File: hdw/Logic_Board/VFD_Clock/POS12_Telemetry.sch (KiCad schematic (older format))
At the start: 9 parts

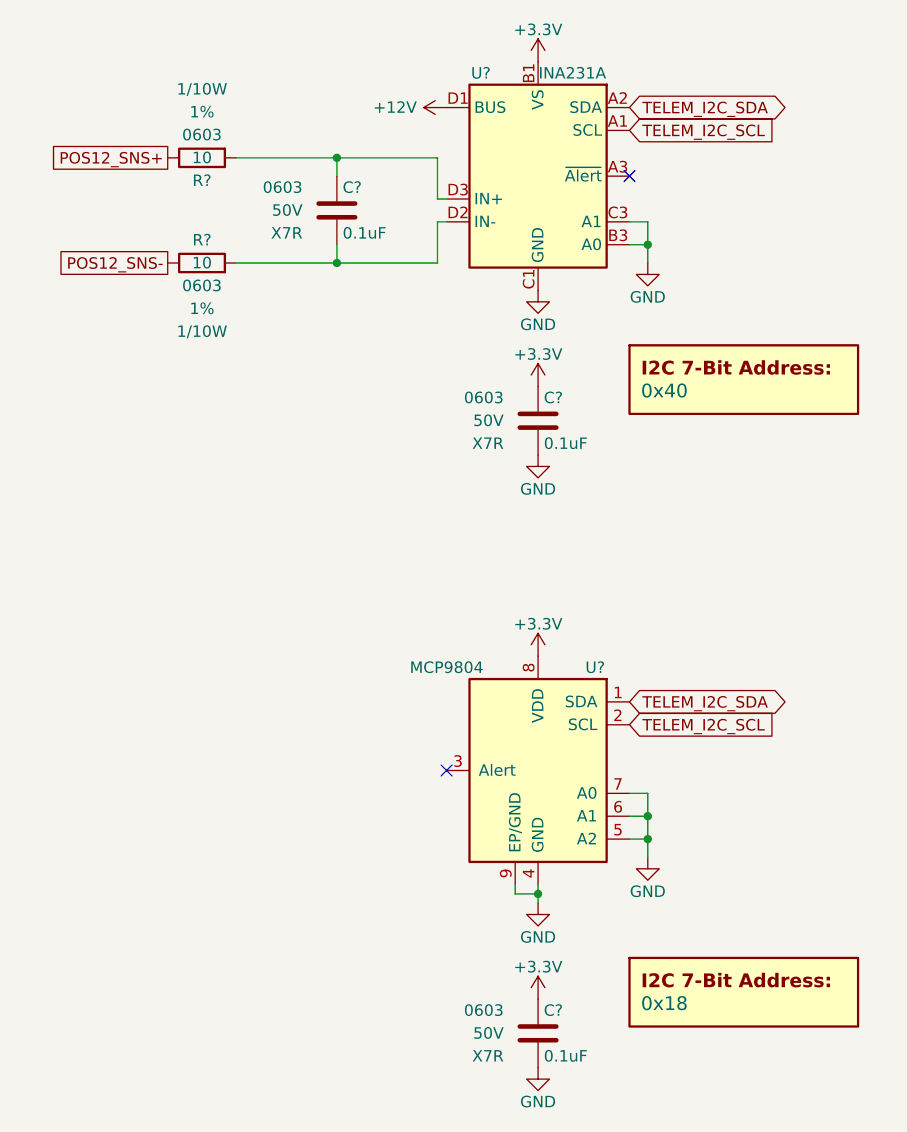
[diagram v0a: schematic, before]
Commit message: Lots of schematic additions
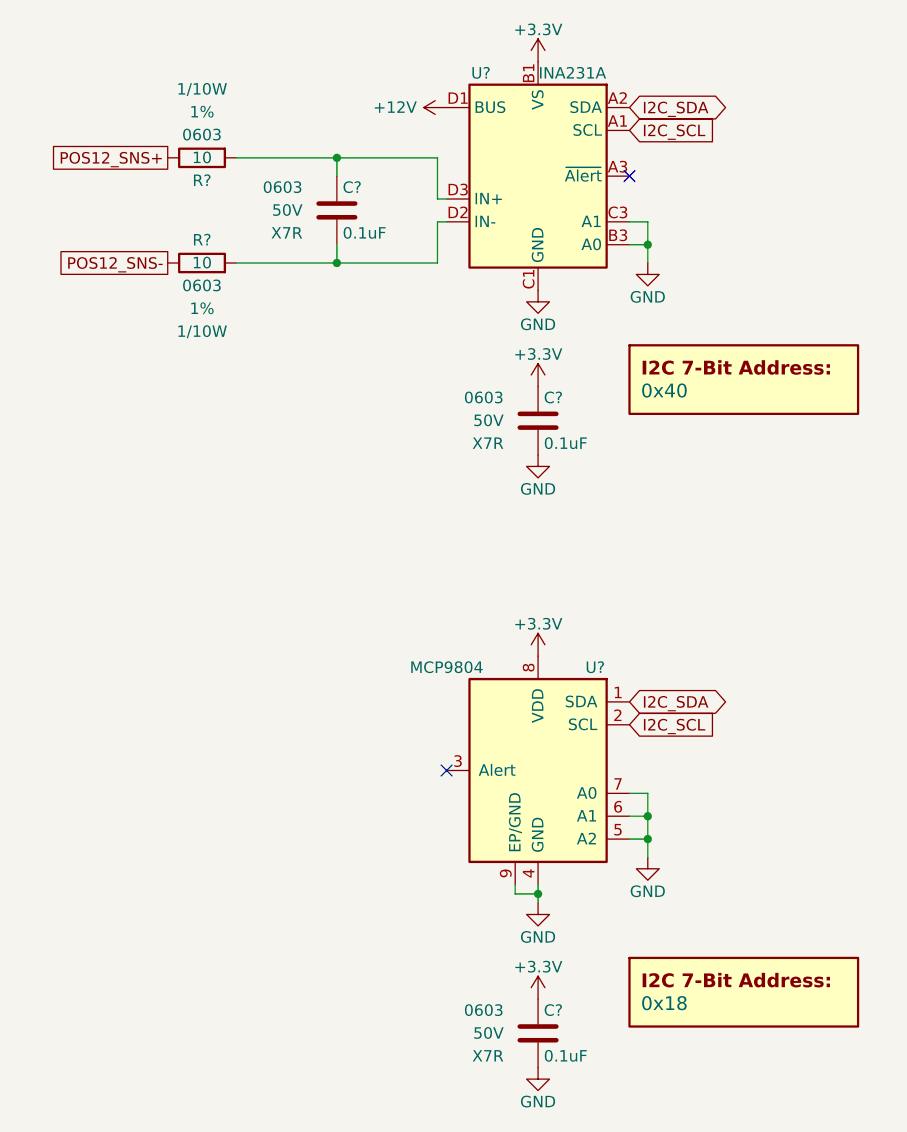
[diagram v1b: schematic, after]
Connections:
- net TELEM_I2C_SCL renamed I2C_SCL
- net TELEM_I2C_SDA renamed I2C_SDA
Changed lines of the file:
@@
 $Descr A 11000 8500
 encoding utf-8
-Sheet 26 26
+Sheet 17 28
 Title ""
 Date ""
@@
 $EndComp
 Text GLabel 5510 1740 2    50   Input ~ 0
-TELEM_I2C_SCL
+I2C_SCL
 $Comp
 L Custom_Library:C_Custom C?
@@
 $EndComp
 Text GLabel 5510 1640 2    50   BiDi ~ 0
-TELEM_I2C_SDA
+I2C_SDA
 NoConn ~ 5510 1940
 $Comp
@@
 $EndComp
 Text GLabel 5510 4340 2    50   Input ~ 0
-TELEM_I2C_SCL
+I2C_SCL
 Text GLabel 5510 4240 2    50   BiDi ~ 0
-TELEM_I2C_SDA
+I2C_SDA
 NoConn ~ 4710 4540
 $Comp

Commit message: Added backup RTC, IO connector, other stuff
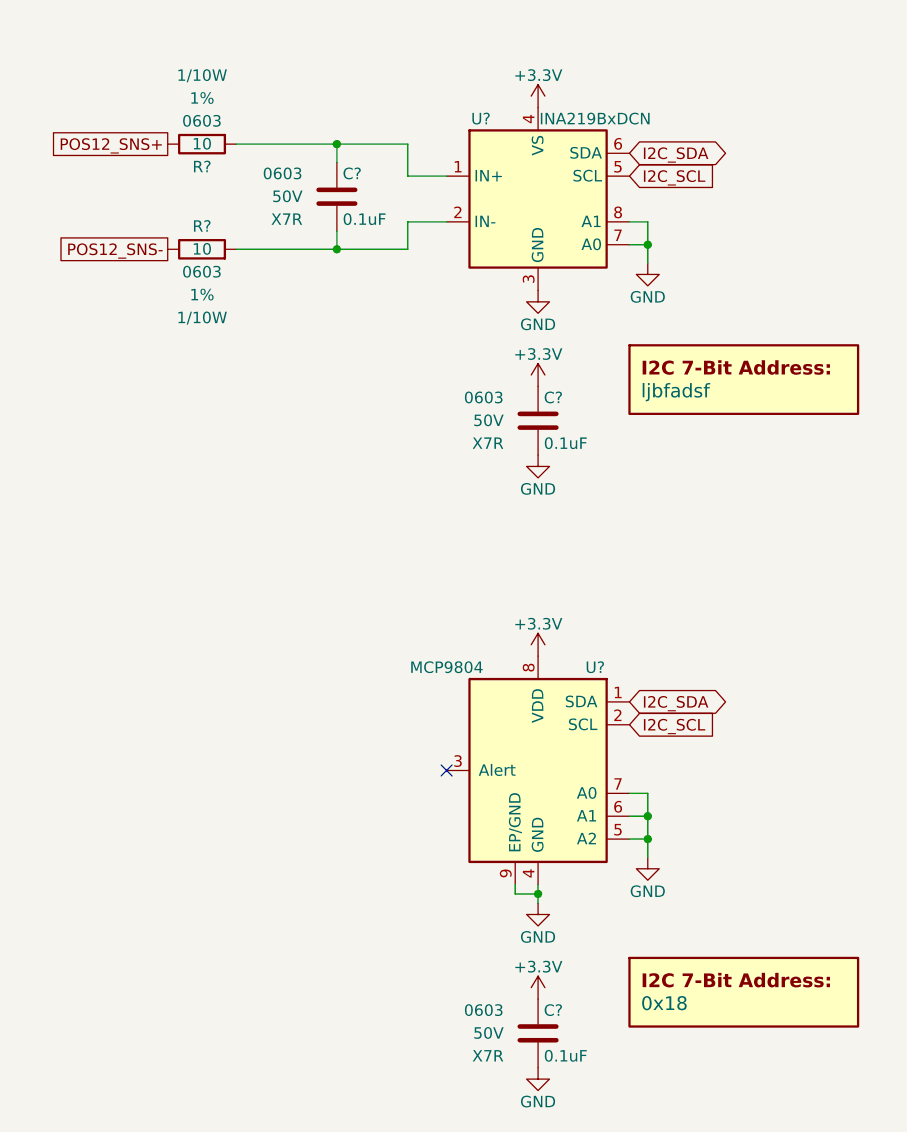
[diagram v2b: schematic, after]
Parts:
- removed U?: INA231A, Custom Footprints Library:Texas_DSBGA-12_1.65x1.39mm_Layout3x4_P0.4mm, symbol Custom_Library:INA231A
- added U?: INA219BxDCN, Package_TO_SOT_SMD:SOT-23-8, symbol Analog_ADC:INA219BxDCN
- DOC?: value 0x40 -> ljbfadsf
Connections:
- net +3V3: now also U?.4 (VS)
- net GND: now also U?.3 (GND), U?.7 (A0), U?.8 (A1)
- net I2C_SCL: now also U?.5 (SCL)
- net I2C_SDA: now also U?.6 (SDA)
- net at C?.2, R?.1: now also U?.2 (IN-)
- net at C?.1, R?.1: now also U?.1 (IN+)
- no-connect marks 2 -> 1
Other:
- moved on the sheet: C?, R?
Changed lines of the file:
@@
 $Descr A 11000 8500
 encoding utf-8
-Sheet 17 28
+Sheet 17 29
 Title ""
 Date ""
@@
 Comment4 ""
 $EndDescr
-$Comp
-L Custom_Library:INA231A U?
-U 1 1 5E073058
-P 5110 1940
-AR Path="/5E0652BA/5E073058" Ref="U?"  Part="1"
-AR Path="/5E0A0E29/5E073058" Ref="U?"  Part="1"
-AR Path="/5E052856/5E073058" Ref="U?"  Part="1"
-F 0 "U?" H 4860 2390 50  0000 C CNN
-F 1 "INA231A" H 5260 2390 50  0000 C CNN
-F 2 "Custom Footprints Library:Texas_DSBGA-12_1.65x1.39mm_Layout3x4_P0.4mm" H 5910 1490 50  0001 C CNN
-F 3 "http://www.ti.com/lit/ds/symlink/ina231.pdf" H 5460 1840 50  0001 C CNN
-F 4 "296-41263-1-ND" H 5110 1940 50  0001 C CNN "Digi-Key PN"
-	1    5110 1940
-	1    0    0    -1
-$EndComp
-Text GLabel 3490 1860 0    50   UnSpc ~ 0
+Text GLabel 3490 1800 0    50   UnSpc ~ 0
 POS12_SNS+
-Text GLabel 3490 2320 0    50   UnSpc ~ 0
+Text GLabel 3490 2260 0    50   UnSpc ~ 0
 POS12_SNS-
 $Comp
@@
 L power:+3.3V #PWR?
 U 1 1 5E0AD665
-P 5110 1440
+P 5110 1640
 AR Path="/5E0652BA/5E0AD665" Ref="#PWR?"  Part="1"
 AR Path="/5E0A0E29/5E0AD665" Ref="#PWR?"  Part="1"
 AR Path="/5E052856/5E0AD665" Ref="#PWR?"  Part="1"
-F 0 "#PWR?" H 5110 1290 50  0001 C CNN
-F 1 "+3.3V" H 5110 1580 50  0000 C CNN
-F 2 "" H 5110 1440 50  0001 C CNN
-F 3 "" H 5110 1440 50  0001 C CNN
-	1    5110 1440
-	1    0    0    -1
-$EndComp
-$Comp
-L power:+12V #PWR?
-U 1 1 5E0AD80E
-P 4710 1640
-AR Path="/5E0652BA/5E0AD80E" Ref="#PWR?"  Part="1"
-AR Path="/5E0A0E29/5E0AD80E" Ref="#PWR?"  Part="1"
-AR Path="/5E052856/5E0AD80E" Ref="#PWR?"  Part="1"
-F 0 "#PWR?" H 4710 1490 50  0001 C CNN
-F 1 "+12V" V 4710 1770 50  0000 L CNN
-F 2 "" H 4710 1640 50  0001 C CNN
-F 3 "" H 4710 1640 50  0001 C CNN
-	1    4710 1640
-	0    -1   -1   0
-$EndComp
-Text GLabel 5510 1740 2    50   Input ~ 0
+F 0 "#PWR?" H 5110 1490 50  0001 C CNN
+F 1 "+3.3V" H 5110 1780 50  0000 C CNN
+F 2 "" H 5110 1640 50  0001 C CNN
+F 3 "" H 5110 1640 50  0001 C CNN
+	1    5110 1640
+	1    0    0    -1
+$EndComp
+Text GLabel 5510 1940 2    50   Input ~ 0
 I2C_SCL
 $Comp
@@
 	1    0    0    -1
 $EndComp
-Text GLabel 5510 1640 2    50   BiDi ~ 0
+Text GLabel 5510 1840 2    50   BiDi ~ 0
 I2C_SDA
-NoConn ~ 5510 1940
 $Comp
 L Custom_Library:I2C_Address DOC?
@@
 AR Path="/5E052856/5E0B8BC8" Ref="DOC?"  Part="1"
 F 0 "DOC?" H 6010 3130 60  0001 C CNN
-F 1 "0x40" H 5560 2880 60  0000 L CNN
+F 1 "ljbfadsf" H 5560 2880 60  0000 L CNN
 F 2 "" H 6010 3230 60  0001 C CNN
 F 3 "" H 6010 3230 60  0001 C CNN
@@
 	5590 4840 5590 4740
 Wire Wire Line
-	4230 2320 4230 2240
-Wire Wire Line
-	4230 1940 4230 1860
-Wire Wire Line
-	4230 2320 4670 2320
-Wire Wire Line
-	4670 2320 4670 2140
-Wire Wire Line
-	4670 2140 4710 2140
-Connection ~ 4230 2320
-Wire Wire Line
-	4230 1860 4670 1860
-Wire Wire Line
-	4670 1860 4670 2040
-Wire Wire Line
-	4670 2040 4710 2040
+	4230 2260 4230 2180
+Wire Wire Line
+	4230 1880 4230 1800
 $Comp
 L Custom_Library:C_Custom C?
 U 1 1 5E07E0FD
-P 4230 2090
+P 4230 2030
 AR Path="/5B3E071A/5E07E0FD" Ref="C?"  Part="1"
 AR Path="/5E0652BA/5E07E0FD" Ref="C?"  Part="1"
 AR Path="/5E0A0E29/5E07E0FD" Ref="C?"  Part="1"
 AR Path="/5E052856/5E07E0FD" Ref="C?"  Part="1"
-F 0 "C?" H 4255 2190 50  0000 L CNN
-F 1 "0.1uF" H 4255 1990 50  0000 L CNN
-F 2 "Capacitors_SMD:C_0603" H 4268 1940 50  0001 C CNN
-F 3 "" H 4255 2190 50  0001 C CNN
-F 4 "0603" H 4080 2190 50  0000 R CNN "display_footprint"
-F 5 "50V" H 4080 2090 50  0000 R CNN "Voltage"
-F 6 "X7R" H 4080 1990 50  0000 R CNN "Dielectric"
-F 7 "399-6856-1-ND" H 320 -4790 50  0001 C CNN "Digi-Key PN"
-	1    4230 2090
+F 0 "C?" H 4255 2130 50  0000 L CNN
+F 1 "0.1uF" H 4255 1930 50  0000 L CNN
+F 2 "Capacitors_SMD:C_0603" H 4268 1880 50  0001 C CNN
+F 3 "" H 4255 2130 50  0001 C CNN
+F 4 "0603" H 4080 2130 50  0000 R CNN "display_footprint"
+F 5 "50V" H 4080 2030 50  0000 R CNN "Voltage"
+F 6 "X7R" H 4080 1930 50  0000 R CNN "Dielectric"
+F 7 "399-6856-1-ND" H 320 -4850 50  0001 C CNN "Digi-Key PN"
+	1    4230 2030
 	1    0    0    -1
 $EndComp
@@
 L Custom_Library:R_Custom R?
 U 1 1 5E082EBB
-P 3640 2320
+P 3640 2260
 AR Path="/5CB6F1ED/5E082EBB" Ref="R?"  Part="1"
 AR Path="/5E0652BA/5E082EBB" Ref="R?"  Part="1"
 AR Path="/5E0A0E29/5E082EBB" Ref="R?"  Part="1"
 AR Path="/5E052856/5E082EBB" Ref="R?"  Part="1"
-F 0 "R?" V 3540 2320 50  0000 C CNN
-F 1 "10" V 3640 2320 50  0000 C CNN
-F 2 "Resistors_SMD:R_0603" H 3640 2320 50  0001 C CNN
-F 3 "" H 3640 2320 50  0001 C CNN
-F 4 "YAG3351CT-ND" H 3940 2720 60  0001 C CNN "Digi-Key PN"
-F 5 "0603" V 3740 2320 50  0000 C CNN "display_footprint"
-F 6 "1%" V 3840 2320 50  0000 C CNN "Tolerance"
-F 7 "1/10W" V 3940 2320 50  0000 C CNN "Wattage"
-	1    3640 2320
+F 0 "R?" V 3540 2260 50  0000 C CNN
+F 1 "10" V 3640 2260 50  0000 C CNN
+F 2 "Resistors_SMD:R_0603" H 3640 2260 50  0001 C CNN
+F 3 "" H 3640 2260 50  0001 C CNN
+F 4 "YAG3351CT-ND" H 3940 2660 60  0001 C CNN "Digi-Key PN"
+F 5 "0603" V 3740 2260 50  0000 C CNN "display_footprint"
+F 6 "1%" V 3840 2260 50  0000 C CNN "Tolerance"
+F 7 "1/10W" V 3940 2260 50  0000 C CNN "Wattage"
+	1    3640 2260
 	0    1    1    0
 $EndComp
 Wire Wire Line
-	3790 2320 4230 2320
+	3790 2260 4230 2260
 $Comp
 L Custom_Library:R_Custom R?
 U 1 1 5E083C4C
-P 3640 1860
+P 3640 1800
 AR Path="/5CB6F1ED/5E083C4C" Ref="R?"  Part="1"
 AR Path="/5E0652BA/5E083C4C" Ref="R?"  Part="1"
 AR Path="/5E0A0E29/5E083C4C" Ref="R?"  Part="1"
 AR Path="/5E052856/5E083C4C" Ref="R?"  Part="1"
-F 0 "R?" V 3540 1860 50  0000 C CNN
-F 1 "10" V 3640 1860 50  0000 C CNN
-F 2 "Resistors_SMD:R_0603" H 3640 1860 50  0001 C CNN
-F 3 "" H 3640 1860 50  0001 C CNN
-F 4 "YAG3351CT-ND" H 3940 2260 60  0001 C CNN "Digi-Key PN"
-F 5 "0603" V 3740 1860 50  0000 C CNN "display_footprint"
-F 6 "1%" V 3840 1860 50  0000 C CNN "Tolerance"
-F 7 "1/10W" V 3940 1860 50  0000 C CNN "Wattage"
-	1    3640 1860
+F 0 "R?" V 3540 1800 50  0000 C CNN
+F 1 "10" V 3640 1800 50  0000 C CNN
+F 2 "Resistors_SMD:R_0603" H 3640 1800 50  0001 C CNN
+F 3 "" H 3640 1800 50  0001 C CNN
+F 4 "YAG3351CT-ND" H 3940 2200 60  0001 C CNN "Digi-Key PN"
+F 5 "0603" V 3740 1800 50  0000 C CNN "display_footprint"
+F 6 "1%" V 3840 1800 50  0000 C CNN "Tolerance"
+F 7 "1/10W" V 3940 1800 50  0000 C CNN "Wattage"
+	1    3640 1800
 	0    1    -1   0
 $EndComp
 Wire Wire Line
-	3790 1860 4230 1860
-Connection ~ 4230 1860
+	3790 1800 4230 1800
+$Comp
+L Analog_ADC:INA219BxDCN U?
+U 1 1 5E1AAC3C
+P 5110 2040
+F 0 "U?" H 4860 2390 50  0000 C CNN
+F 1 "INA219BxDCN" H 5360 2390 50  0000 C CNN
+F 2 "Package_TO_SOT_SMD:SOT-23-8" H 5760 1690 50  0001 C CNN
+F 3 "http://www.ti.com/lit/ds/symlink/ina219.pdf" H 5460 1940 50  0001 C CNN
+F 4 "296-46420-1-ND" H 5110 2040 50  0001 C CNN "Digi-Key PN"
+	1    5110 2040
+	1    0    0    -1
+$EndComp
+Wire Wire Line
+	4710 1940 4540 1940
+Wire Wire Line
+	4540 1940 4540 1800
+Wire Wire Line
+	4540 1800 4230 1800
+Connection ~ 4230 1800
+Wire Wire Line
+	4710 2140 4540 2140
+Wire Wire Line
+	4540 2140 4540 2260
+Wire Wire Line
+	4540 2260 4230 2260
+Connection ~ 4230 2260
 $EndSCHEMATC

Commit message: Changed to configurable discrete gates, added VBAT stuff
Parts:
- removed C?: 0.1uF, Capacitors_SMD:C_0603, symbol Custom_Library:C_Custom
- removed DOC?: 0x18, symbol Custom_Library:I2C_Address
- removed U?: MCP9804, Package_DFN_QFN:DFN-8-1EP_3x2mm_P0.5mm_EP1.3x1.5mm, symbol Sensor_Temperature:MCP9804_DFN
- added C?: 0.1uF, Capacitors_SMD:C_0603, symbol Custom_Library:C_Custom
- added DOC?: 0x18, symbol Custom_Library:I2C_Address
- added U?: MCP9804, Package_DFN_QFN:DFN-8-1EP_3x2mm_P0.5mm_EP1.3x1.5mm, symbol Sensor_Temperature:MCP9804_DFN
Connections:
- net +3V3: now also C?.1, U?.8 (VDD)
- net GND: now also C?.2, U?.4 (GND), U?.5 (A2), U?.6 (A1), U?.7 (A0), U?.9 (EP/GND)
- net I2C_SCL: now also U?.2 (SCL)
- net I2C_SDA: now also U?.1 (SDA)
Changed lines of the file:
@@
 $Comp
 L power:GND #PWR?
-U 1 1 5E0BDB8A
+U 1 1 5E2AA995
 P 5110 5120
-AR Path="/5B3E071A/5E0BDB8A" Ref="#PWR?"  Part="1"
-AR Path="/5E0652BA/5E0BDB8A" Ref="#PWR?"  Part="1"
-AR Path="/5E0A0E29/5E0BDB8A" Ref="#PWR?"  Part="1"
-AR Path="/5E052856/5E0BDB8A" Ref="#PWR?"  Part="1"
+AR Path="/5B3E071A/5E2AA995" Ref="#PWR?"  Part="1"
+AR Path="/5E0652BA/5E2AA995" Ref="#PWR?"  Part="1"
+AR Path="/5E0A0E29/5E2AA995" Ref="#PWR?"  Part="1"
+AR Path="/5E052856/5E2AA995" Ref="#PWR?"  Part="1"
 F 0 "#PWR?" H 5110 4870 50  0001 C CNN
 F 1 "GND" H 5110 4970 50  0000 C CNN
@@
 $Comp
 L power:+3.3V #PWR?
-U 1 1 5E0BDB95
+U 1 1 5E2AA99A
 P 5110 4040
-AR Path="/5E0652BA/5E0BDB95" Ref="#PWR?"  Part="1"
-AR Path="/5E0A0E29/5E0BDB95" Ref="#PWR?"  Part="1"
-AR Path="/5E052856/5E0BDB95" Ref="#PWR?"  Part="1"
+AR Path="/5E0652BA/5E2AA99A" Ref="#PWR?"  Part="1"
+AR Path="/5E0A0E29/5E2AA99A" Ref="#PWR?"  Part="1"
+AR Path="/5E052856/5E2AA99A" Ref="#PWR?"  Part="1"
 F 0 "#PWR?" H 5110 3890 50  0001 C CNN
 F 1 "+3.3V" H 5110 4180 50  0000 C CNN
@@
 $Comp
 L Sensor_Temperature:MCP9804_DFN U?
-U 1 1 5E0BDB9D
+U 1 1 5E2AA99D
 P 5110 4540
-AR Path="/5B3E071A/5E0BDB9D" Ref="U?"  Part="1"
-AR Path="/5E0652BA/5E0BDB9D" Ref="U?"  Part="1"
-AR Path="/5E0A0E29/5E0BDB9D" Ref="U?"  Part="1"
-AR Path="/5E052856/5E0BDB9D" Ref="U?"  Part="1"
+AR Path="/5B3E071A/5E2AA99D" Ref="U?"  Part="1"
+AR Path="/5E0652BA/5E2AA99D" Ref="U?"  Part="1"
+AR Path="/5E0A0E29/5E2AA99D" Ref="U?"  Part="1"
+AR Path="/5E052856/5E2AA99D" Ref="U?"  Part="1"
 F 0 "U?" H 4860 4990 50  0000 C CNN
 F 1 "MCP9804" H 5510 4990 50  0000 C CNN
@@
 $Comp
 L Custom_Library:C_Custom C?
-U 1 1 5E0CB7AA
+U 1 1 5E2AA9A1
 P 5110 5690
-AR Path="/5B3E071A/5E0CB7AA" Ref="C?"  Part="1"
-AR Path="/5E0652BA/5E0CB7AA" Ref="C?"  Part="1"
-AR Path="/5E0A0E29/5E0CB7AA" Ref="C?"  Part="1"
-AR Path="/5E052856/5E0CB7AA" Ref="C?"  Part="1"
+AR Path="/5B3E071A/5E2AA9A1" Ref="C?"  Part="1"
+AR Path="/5E0652BA/5E2AA9A1" Ref="C?"  Part="1"
+AR Path="/5E0A0E29/5E2AA9A1" Ref="C?"  Part="1"
+AR Path="/5E052856/5E2AA9A1" Ref="C?"  Part="1"
 F 0 "C?" H 5135 5790 50  0000 L CNN
 F 1 "0.1uF" H 5135 5590 50  0000 L CNN
@@
 $Comp
 L power:+3.3V #PWR?
-U 1 1 5E0CB7B0
+U 1 1 5E2AA9A6
 P 5110 5540
-AR Path="/5E0652BA/5E0CB7B0" Ref="#PWR?"  Part="1"
-AR Path="/5E0A0E29/5E0CB7B0" Ref="#PWR?"  Part="1"
-AR Path="/5E052856/5E0CB7B0" Ref="#PWR?"  Part="1"
+AR Path="/5E0652BA/5E2AA9A6" Ref="#PWR?"  Part="1"
+AR Path="/5E0A0E29/5E2AA9A6" Ref="#PWR?"  Part="1"
+AR Path="/5E052856/5E2AA9A6" Ref="#PWR?"  Part="1"
 F 0 "#PWR?" H 5110 5390 50  0001 C CNN
 F 1 "+3.3V" H 5110 5680 50  0000 C CNN
@@
 $Comp
 L power:GND #PWR?
-U 1 1 5E0CB7B6
+U 1 1 5E2AA9AD
 P 5110 5840
-AR Path="/5E0652BA/5E0CB7B6" Ref="#PWR?"  Part="1"
-AR Path="/5E0A0E29/5E0CB7B6" Ref="#PWR?"  Part="1"
-AR Path="/5E052856/5E0CB7B6" Ref="#PWR?"  Part="1"
+AR Path="/5E0652BA/5E2AA9AD" Ref="#PWR?"  Part="1"
+AR Path="/5E0A0E29/5E2AA9AD" Ref="#PWR?"  Part="1"
+AR Path="/5E052856/5E2AA9AD" Ref="#PWR?"  Part="1"
 F 0 "#PWR?" H 5110 5590 50  0001 C CNN
 F 1 "GND" H 5110 5690 50  0000 C CNN
@@
 $Comp
 L Custom_Library:I2C_Address DOC?
-U 1 1 5E0CB7BC
+U 1 1 5E2AA9AF
 P 6010 5560
-AR Path="/5E0652BA/5E0CB7BC" Ref="DOC?"  Part="1"
-AR Path="/5E0A0E29/5E0CB7BC" Ref="DOC?"  Part="1"
-AR Path="/5E052856/5E0CB7BC" Ref="DOC?"  Part="1"
+AR Path="/5E0652BA/5E2AA9AF" Ref="DOC?"  Part="1"
+AR Path="/5E0A0E29/5E2AA9AF" Ref="DOC?"  Part="1"
+AR Path="/5E052856/5E2AA9AF" Ref="DOC?"  Part="1"
 F 0 "DOC?" H 6010 5810 60  0001 C CNN
 F 1 "0x18" H 5560 5560 60  0000 L CNN
